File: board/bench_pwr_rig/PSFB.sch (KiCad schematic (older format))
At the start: 170 parts, among them Q10 BSS138, Q11 STP110N10F7, Q12 STP110N10F7, Q13 BSS138, Q14 BSS138, Q15 STP110N10F7, Q16 STP110N10F7, Q5 MMBT3906, Q6 STF26N60M2, Q7 STF26N60M2, Q8 STF26N60M2, Q9 STF26N60M2, T1 CST1211, T2 PQ2625_PROTO, U10 TL431DBZ, U11 FODM217B, U12 ISO7240MDW, U13 UCC27714D, U14 UCC28951, U15 UCC27714D, U16 TLC272, U17 AGP2923-333, U18 UCC27714D, U19 OPA376xxDBV, U8 LM78L05_TO92, U9 UCC27714D

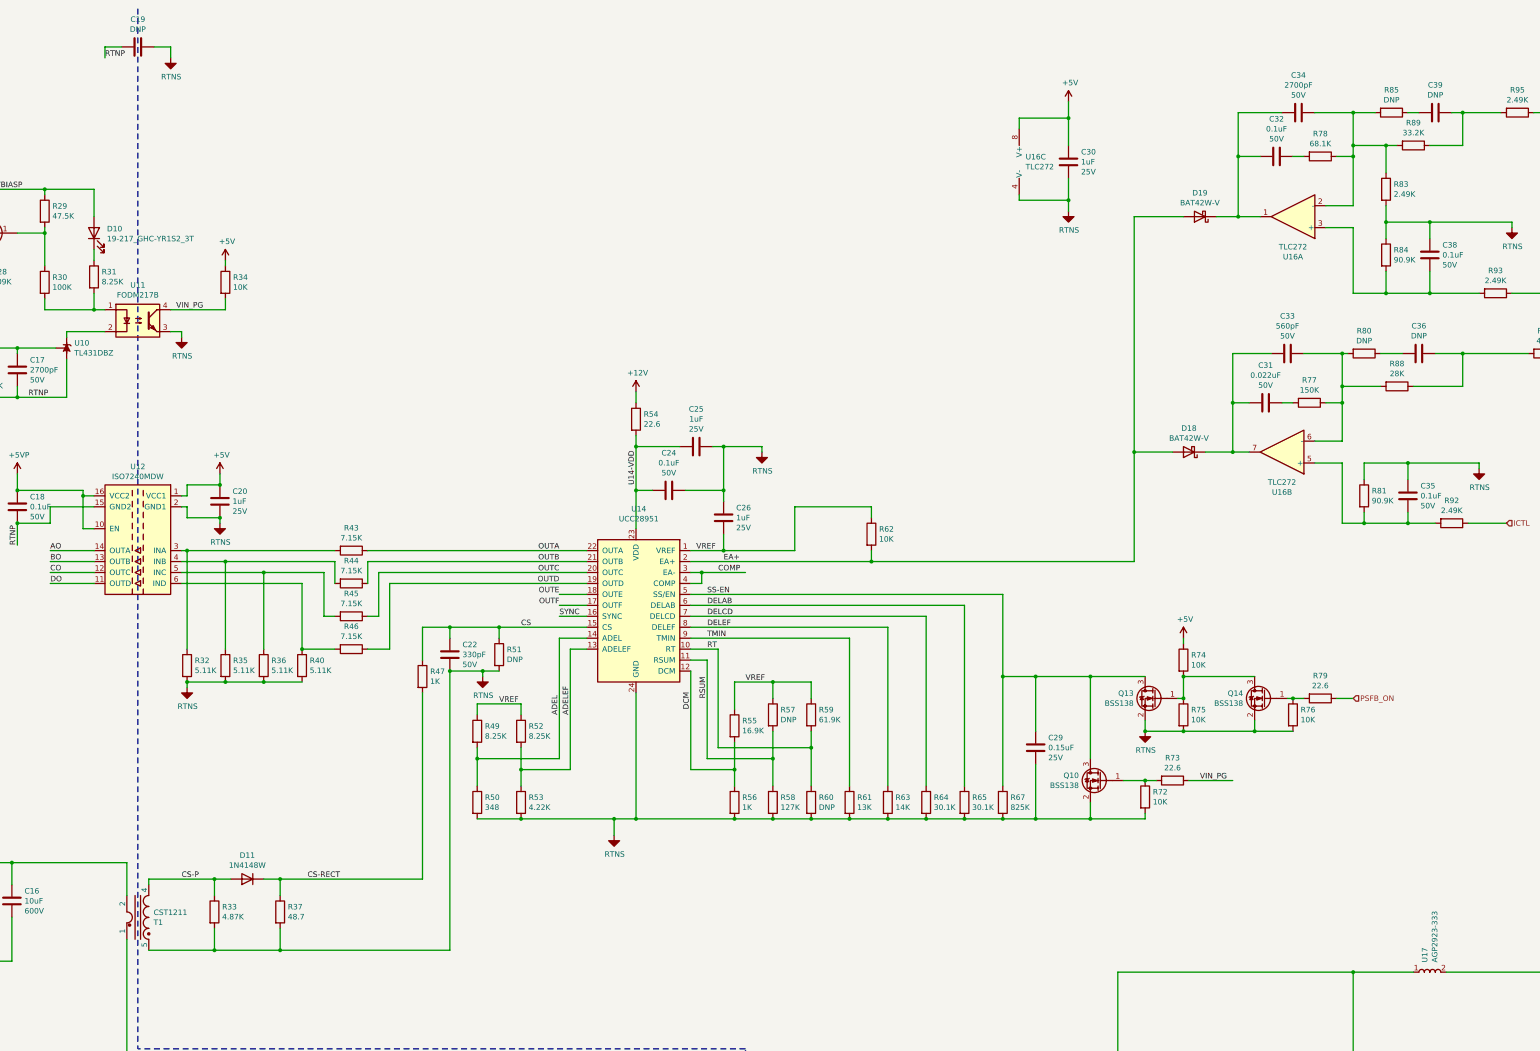
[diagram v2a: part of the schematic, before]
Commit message: Updated layout
Added output screw terminal
Added mounting screws M4
Changed primary ground to secondary ground plane coupling capacitor to radial disc type with safety rating X1, Y1
Continued layout
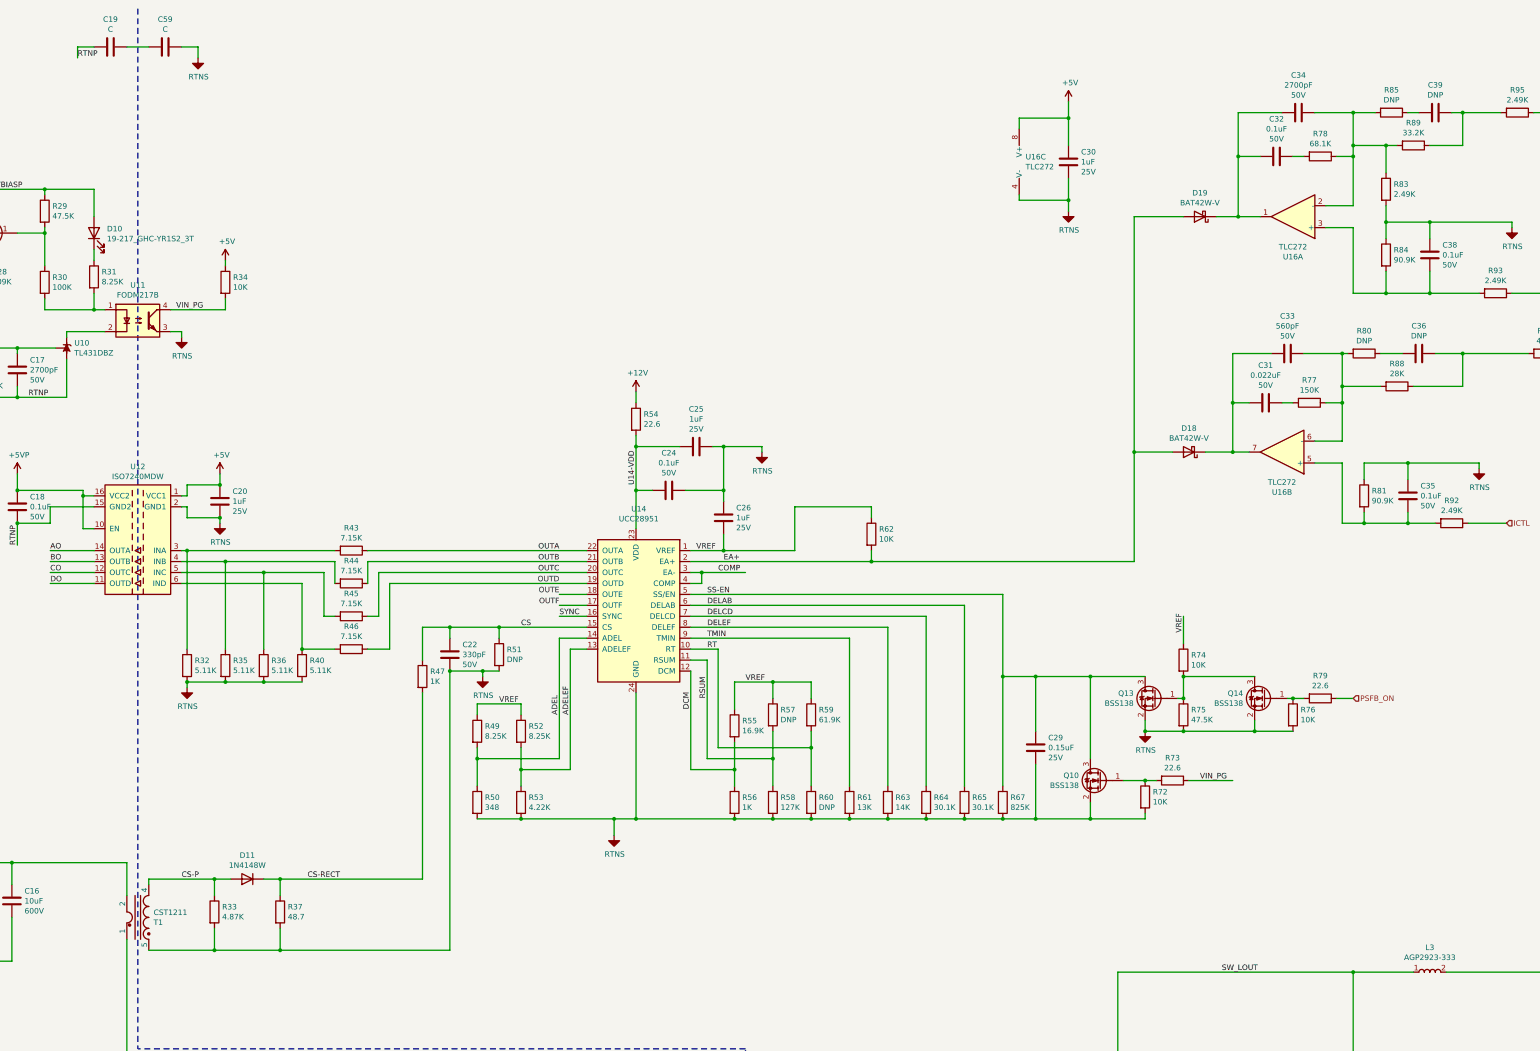
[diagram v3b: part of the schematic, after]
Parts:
- removed R75: CRCW060310K0FKEA, Resistor_SMD:R_0603_1608Metric_Pad1.05x0.95mm_HandSolder, symbol Resistor:CRCW060310K0FKEA
- removed U17: AGP2923-333, Inductor_THT:L_Coilcraft_AGP2923, symbol Inductor:AGP2923-333
- added C59: C, Capacitor_THT:C_Disc_D9.0mm_W5.0mm_P10.00mm, symbol Device:C
- added L3: AGP2923-333, Inductor_THT:L_Coilcraft_AGP2923, symbol Inductor:AGP2923-333
- added R75: 0603WAF4752T5E, Resistor_SMD:R_0603_1608Metric_Pad1.05x0.95mm_HandSolder, symbol Resistor:0603WAF4752T5E
- C19: value DNP -> C; footprint Capacitor_SMD:C_1206_3216Metric -> Capacitor_THT:C_Disc_D9.0mm_W5.0mm_P10.00mm
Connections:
- net +5V: no longer R74.1
- net GND: now also C59.1, R75.2; no longer C19.1
- net OUTP: now also L3.2
- net VREF: now also R74.1
- net SW_LOUT: now reaches Q11.2 (D), Q15.2 (D)
- net SW_LOUT: now also L3.1
- net at Q13.1 (G), Q14.3 (D), R74.2: now also R75.1
- new net: C19.1, C59.2
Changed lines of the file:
@@
 	17700 11100 17700 11150
 $Comp
-L Inductor:AGP2923-333 U17
-U 1 1 5FB02C12
-P 17300 9450
-F 0 "U17" H 17388 9496 50  0000 L CNN
-F 1 "AGP2923-333" H 17388 9405 50  0000 L CNN
-F 2 "Inductor_THT:L_Coilcraft_AGP2923" H 17350 9250 50  0001 C CNN
-F 3 "https://www.coilcraft.com/getmedia/6fe93cdb-fea1-4ec7-9fa6-c6c063686989/agp2923.pdf" H 17350 9250 50  0001 C CNN
-	1    17300 9450
-	0    -1   -1   0
-$EndComp
-$Comp
 L Inductor:SER1512-103 L1
 U 1 1 5FB5FBBB
@@
 Text HLabel 21950 10400 2    50   UnSpc ~ 0
 OUTN
-$Comp
-L Device:C C19
-U 1 1 6173280E
-P 5500 1000
-F 0 "C19" V 5248 1000 50  0000 C CNN
-F 1 "DNP" V 5339 1000 50  0000 C CNN
-F 2 "Capacitor_SMD:C_1206_3216Metric" H 5538 850 50  0001 C CNN
-F 3 "~" H 5500 1000 50  0001 C CNN
-	1    5500 1000
-	0    1    1    0
-$EndComp
-Wire Wire Line
-	5350 1000 5200 1000
-Wire Wire Line
-	5200 1000 5200 1100
 Wire Wire Line
-	5650 1000 5800 1000
+	5100 1000 4950 1000
 Wire Wire Line
-	5800 1000 5800 1100
+	4950 1000 4950 1100
 $Comp
 L Device:R R82
@@
 	16850 15300 16850 15450
 $Comp
-L power:RTNS #PWR036
-U 1 1 61B18E6F
-P 5800 1100
-F 0 "#PWR036" H 5800 850 50  0001 C CNN
-F 1 "RTNS" H 5805 927 50  0000 C CNN
-F 2 "" H 5800 1100 50  0001 C CNN
-F 3 "" H 5800 1100 50  0001 C CNN
-	1    5800 1100
-	1    0    0    -1
-$EndComp
-$Comp
 L power:RTNS #PWR047
 U 1 1 61B19F7D
@@
 Wire Wire Line
 	14200 6750 14200 7500
-$Comp
-L Resistor:CRCW060310K0FKEA R75
-U 1 1 6150AC7C
-P 15050 7100
-F 0 "R75" H 15120 7146 50  0000 L CNN
-F 1 "CRCW060310K0FKEA" H 15550 6850 50  0001 C CNN
-F 2 "Resistor_SMD:R_0603_1608Metric_Pad1.05x0.95mm_HandSolder" H 15050 7100 50  0001 C CNN
-F 3 "https://www.vishay.com/docs/20035/dcrcwe3.pdf" H 15050 7100 50  0001 C CNN
-F 4 "10K" H 15120 7055 50  0000 L CNN "Resistance"
-	1    15050 7100
-	1    0    0    -1
-$EndComp
 Wire Wire Line
 	14700 7150 14700 7250
-Wire Wire Line
-	15050 7250 14700 7250
 Connection ~ 14700 7250
 Wire Wire Line
@@
 $EndComp
 $Comp
-L power:+5V #PWR054
-U 1 1 6166AE96
-P 15050 6400
-F 0 "#PWR054" H 15050 6250 50  0001 C CNN
-F 1 "+5V" H 15065 6573 50  0000 C CNN
-F 2 "" H 15050 6400 50  0001 C CNN
-F 3 "" H 15050 6400 50  0001 C CNN
-	1    15050 6400
-	1    0    0    -1
-$EndComp
-Wire Wire Line
-	15050 6400 15050 6450
-Connection ~ 15050 6950
-$Comp
 L Transistor_FET:BSS138 Q14
 U 1 1 617719F5
@@
 $EndComp
 Wire Wire Line
-	15700 7250 15050 7250
-Connection ~ 15050 7250
-Wire Wire Line
 	15050 6750 15050 6950
 Wire Wire Line
@@
 Text Label 2600 2050 0    50   ~ 0
 RTNP
-Text Label 5200 1100 0    50   ~ 0
+Text Label 4950 1100 0    50   ~ 0
 RTNP
+Wire Wire Line
+	15050 6200 15050 6450
+Text Label 15050 6350 1    50   ~ 0
+VREF
+$Comp
+L Resistor:0603WAF4752T5E R75
+U 1 1 5FC9AF0F
+P 15050 7100
+F 0 "R75" H 15120 7146 50  0000 L CNN
+F 1 "0603WAF4752T5E" H 15550 6850 50  0001 C CNN
+F 2 "Resistor_SMD:R_0603_1608Metric_Pad1.05x0.95mm_HandSolder" H 15050 7100 50  0001 C CNN
+F 3 "https://datasheet.lcsc.com/szlcsc/Uniroyal-Elec-0603WAF1001T5E_C21190.pdf" H 15050 7100 50  0001 C CNN
+F 4 "47.5K" H 15120 7055 50  0000 L CNN "Resistance"
+	1    15050 7100
+	1    0    0    -1
+$EndComp
+Wire Wire Line
+	14700 7250 15050 7250
+Connection ~ 15050 6950
+Connection ~ 15050 7250
+Wire Wire Line
+	15050 7250 15700 7250
+Text Label 15400 9450 0    50   ~ 0
+SW_LOUT
+$Comp
+L Inductor:AGP2923-333 L3
+U 1 1 5FBC4317
+P 17300 9450
+F 0 "L3" V 17525 9450 50  0000 C CNN
+F 1 "AGP2923-333" V 17434 9450 50  0000 C CNN
+F 2 "Inductor_THT:L_Coilcraft_AGP2923" H 17350 9250 50  0001 C CNN
+F 3 "https://www.coilcraft.com/getmedia/6fe93cdb-fea1-4ec7-9fa6-c6c063686989/agp2923.pdf" H 17350 9250 50  0001 C CNN
+	1    17300 9450
+	0    -1   -1   0
+$EndComp
+$Comp
+L power:RTNS #PWR036
+U 1 1 61B18E6F
+P 6050 1100
+F 0 "#PWR036" H 6050 850 50  0001 C CNN
+F 1 "RTNS" H 6055 927 50  0000 C CNN
+F 2 "" H 6050 1100 50  0001 C CNN
+F 3 "" H 6050 1100 50  0001 C CNN
+	1    6050 1100
+	1    0    0    -1
+$EndComp
+Wire Wire Line
+	6050 1000 6050 1100
+Wire Wire Line
+	5900 1000 6050 1000
+$Comp
+L Device:C C59
+U 1 1 601D867B
+P 5750 1000
+F 0 "C59" V 5498 1000 50  0000 C CNN
+F 1 "C" V 5589 1000 50  0000 C CNN
+F 2 "Capacitor_THT:C_Disc_D9.0mm_W5.0mm_P10.00mm" H 5788 850 50  0001 C CNN
+F 3 "~" H 5750 1000 50  0001 C CNN
+	1    5750 1000
+	0    1    1    0
+$EndComp
+$Comp
+L Device:C C19
+U 1 1 601D8067
+P 5250 1000
+F 0 "C19" V 4998 1000 50  0000 C CNN
+F 1 "C" V 5089 1000 50  0000 C CNN
+F 2 "Capacitor_THT:C_Disc_D9.0mm_W5.0mm_P10.00mm" H 5288 850 50  0001 C CNN
+F 3 "~" H 5250 1000 50  0001 C CNN
+	1    5250 1000
+	0    1    1    0
+$EndComp
+Wire Wire Line
+	5400 1000 5600 1000
 $EndSCHEMATC
